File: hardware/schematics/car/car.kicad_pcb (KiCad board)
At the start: 12 copper layers, 17.9 x 30.2 mm, 20 parts, among them M1 Motor_Servo, Q1 PMOS, SW1 SW_SPST, SW2 SW_Push, SW3 SW_Push, U1 VL53L0CXV0DH1, U10 Mini-560, U11 JGA25-37x, U2 VL53L0CXV0DH1, U3 VL53L0CXV0DH1, U4 Pixy2, U6 TB6612FNG, U7 SparkFun OTOS, U9 Mini-360

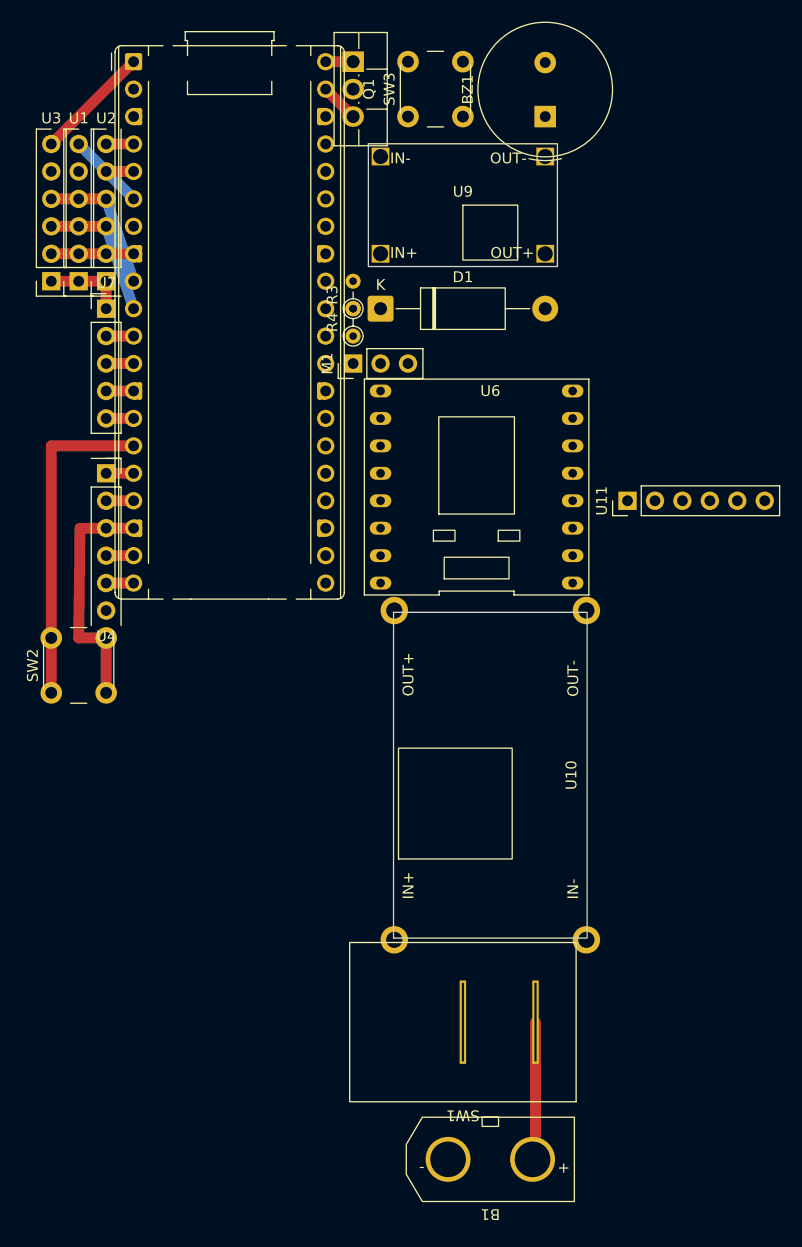
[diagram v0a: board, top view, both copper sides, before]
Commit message: [Schematic] Add ADC cap, place underneath pico it and buzzer.
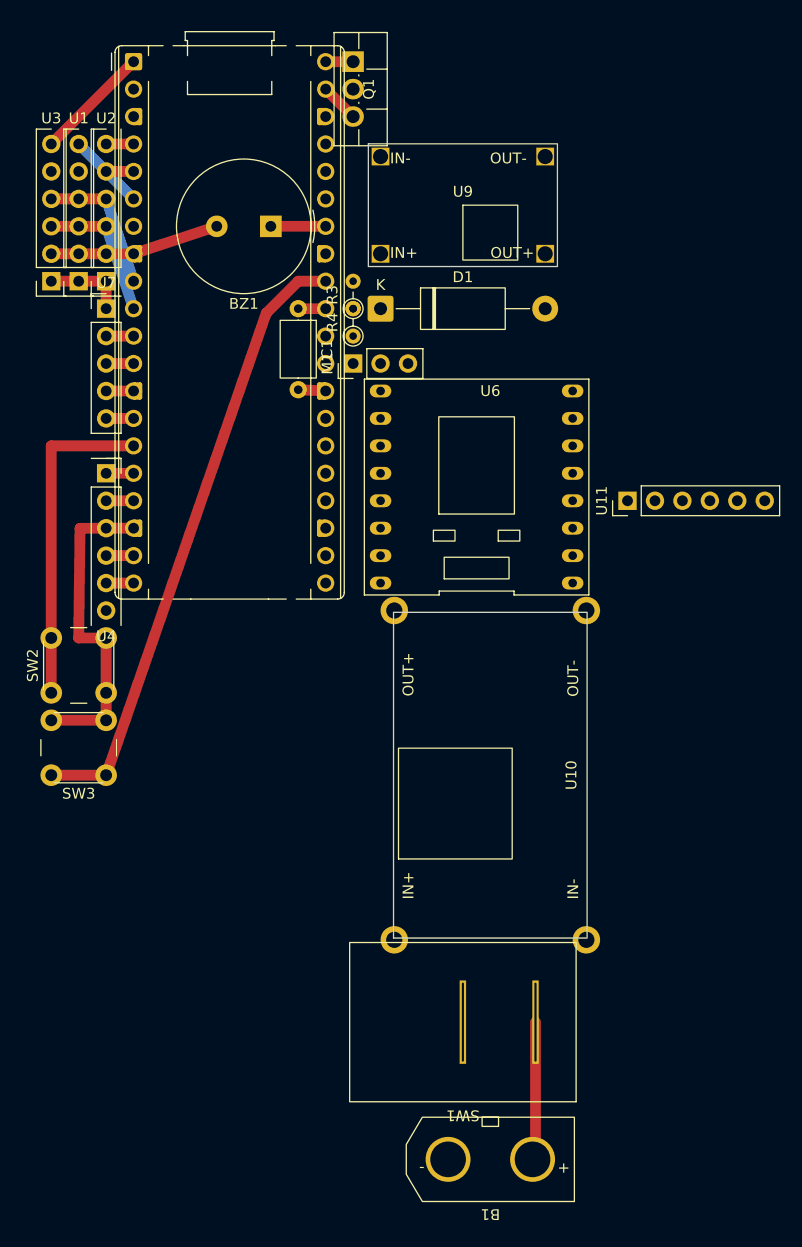
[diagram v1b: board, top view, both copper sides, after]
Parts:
- added C1: 1uF, Capacitor_THT:C_Axial_L5.1mm_D3.1mm_P7.50mm_Horizontal, F.Cu at (142.2, 38.1)
- moved SW3 69.3 mm to (121.9, 78.7), turned to 180 degrees
- moved BZ1 27.4 mm to (139.7, 30.5), turned to 180 degrees
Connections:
- BZ1 pad 1: Net-(A1-GPIO27_ADC1) -> Net-(A1-GPIO28_ADC2)
- SW3 pad 1: Net-(A1-GPIO28_ADC2) -> Net-(A1-GPIO27_ADC1)
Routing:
- net Net-(A1-GPIO27_ADC1): track 0.00 -> 57.1 mm
- net GND: track 152.9 -> 171.2 mm
- net Net-(A1-GPIO28_ADC2): track 0.00 -> 5.08 mm
- net Net-(A1-GPIO26_ADC0): track 0.00 -> 2.54 mm

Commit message: [Schematic] Move a lot, fix mini560 footprint wrong size.
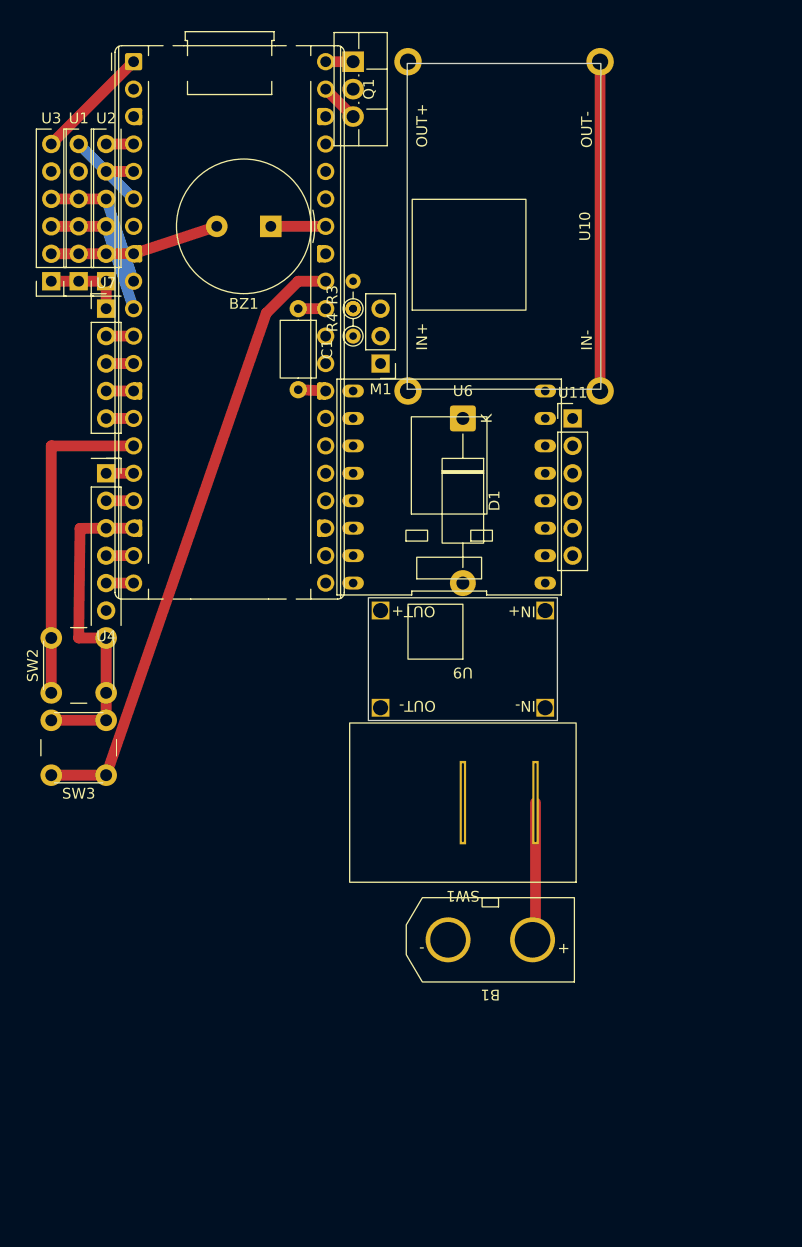
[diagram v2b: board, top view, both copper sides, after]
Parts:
- U11: footprint Connector_PinHeader_2.54mm:PinHeader_1x06_P2.54mm_Vertical -> xlnc-foot:JGA25-37x_PinHeader_1x06_P2.54mm_Vertical
- moved U10 50.8 mm to (161.3, 30.5)
- moved U9 42.0 mm to (157.5, 70.5), turned to 180 degrees
- moved B1 20.3 mm to (160.0, 96.5)
- moved SW1 20.3 mm to (157.5, 83.8)
- moved D1 12.7 mm to (157.5, 48.3), turned to -90 degrees
- moved U11 9.16 mm to (167.6, 48.3), turned to 0 degrees
- moved M1 2.54 mm to (149.9, 43.2), turned to 180 degrees
- moved U6 2.54 mm to (156.2, 54.6)
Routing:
- net GND: track 171.2 -> 241.3 mm
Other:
- board size 17.9 x 30.2 mm -> 17.9 x 30.1 mm

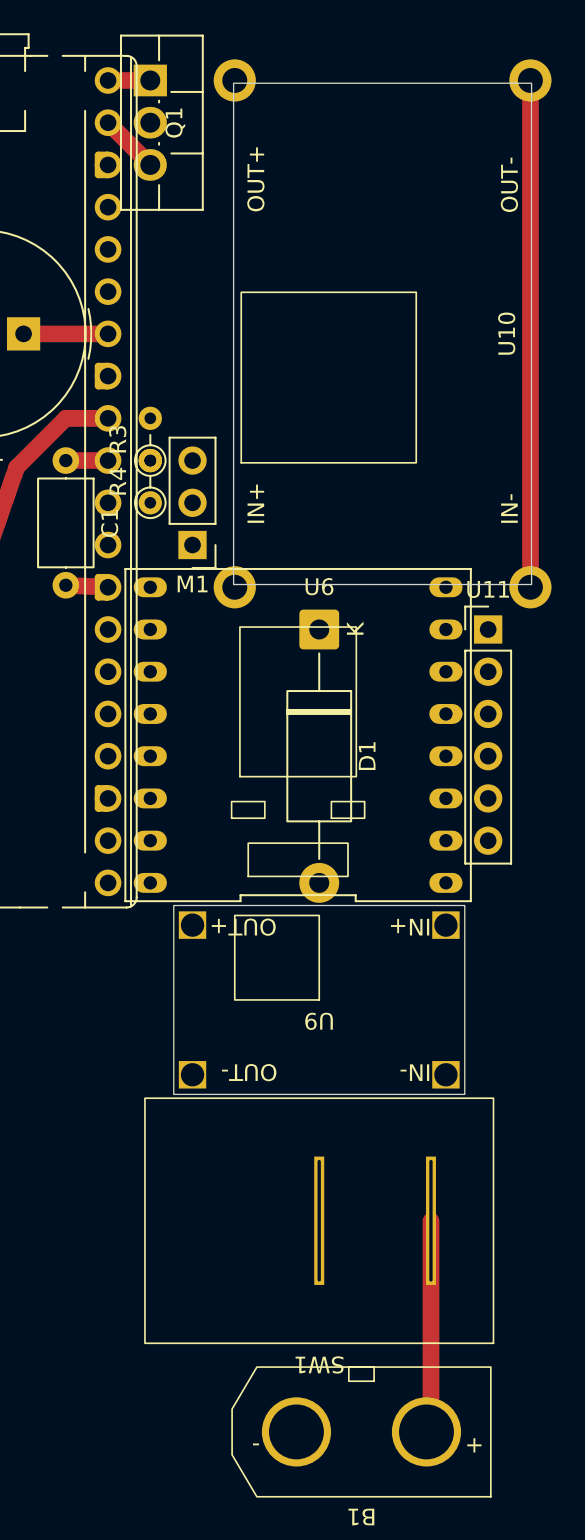
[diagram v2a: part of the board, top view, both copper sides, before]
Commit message: [Schematic] Routed all.
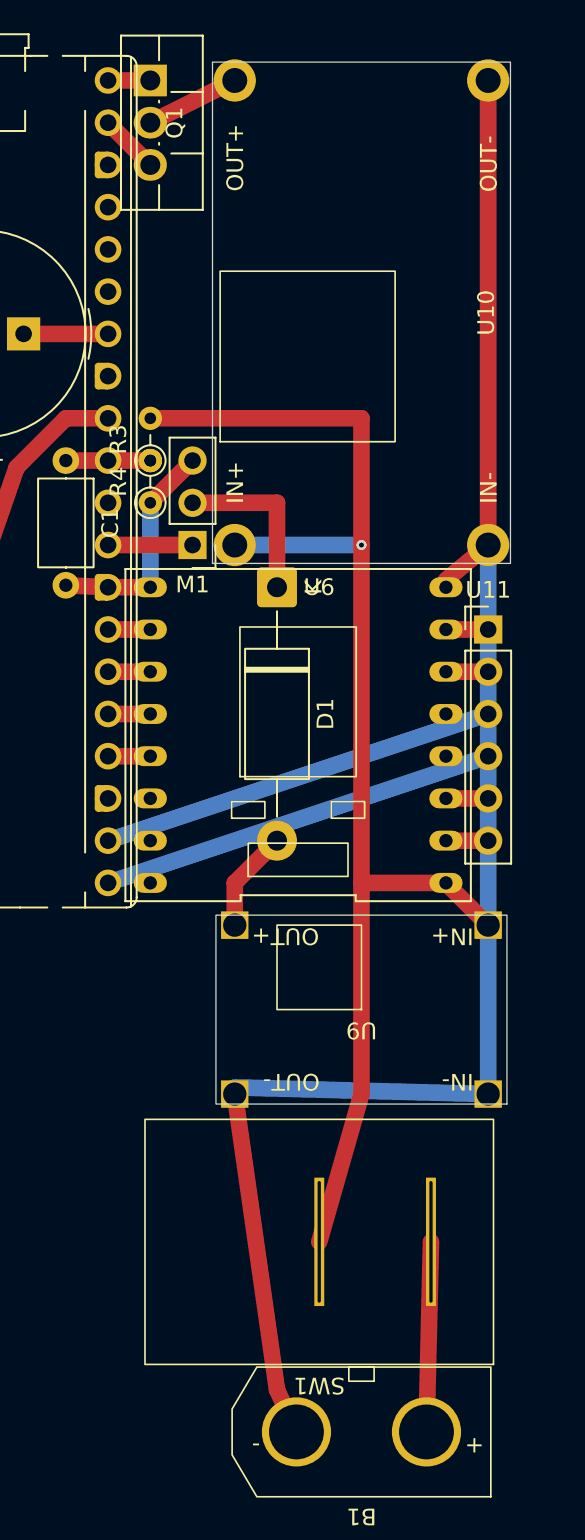
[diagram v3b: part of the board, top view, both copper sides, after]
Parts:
- U9: footprint xlnc-foot:Buck_Mini-360 -> xlnc-foot:Buck_Mini-360_2.54mm
- moved D1 3.59 mm to (154.9, 45.7)
- moved U9 2.61 mm to (160.0, 71.1)
- moved U10 1.80 mm to (160.0, 29.2)
- moved SW1 1.27 mm to (157.5, 85.1)
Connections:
- U11 pad 3: Net-(A1-GPIO20) -> Net-(A1-GPIO16)
- U11 pad 4: Net-(A1-GPIO21) -> Net-(A1-GPIO17)
- U6 pad 1: Net-(U11-M1) -> unconnected-(U6-AO1-Pad1)
- U6 pad 11: unconnected-(U6-BO1-Pad11) -> Net-(U11-M1)
- U6 pad 15: unconnected-(U6-PWMB-Pad15) -> Net-(A1-GPIO21)
- U6 pad 16: unconnected-(U6-BIN2-Pad16) -> Net-(A1-GPIO20)
- U6 pad 17: unconnected-(U6-BIN1-Pad17) -> Net-(A1-GPIO19)
- U6 pad 19: Net-(A1-GPIO16) -> Net-(A1-GPIO18)
- U6 pad 21: Net-(A1-GPIO18) -> unconnected-(U6-AIN1-Pad21)
- U6 pad 22: Net-(A1-GPIO19) -> unconnected-(U6-AIN2-Pad22)
- U6 pad 23: Net-(A1-GPIO17) -> unconnected-(U6-PWMA-Pad23)
- U6 pad 5: Net-(U11-M2) -> unconnected-(U6-AO2-Pad5)
- U6 pad 7: unconnected-(U6-BO2-Pad7) -> Net-(U11-M2)
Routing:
- net VBAT: track 0.00 -> 78.9 mm, vias 0 -> 1
- net GND: track 241.3 -> 318.4 mm
- net +5V: track 0.00 -> 59.1 mm
- net +3.3V: track 30.3 -> 81.2 mm
- net Net-(A1-GPIO17): track 0.00 -> 24.1 mm
- net Net-(A1-GPIO16): track 0.00 -> 24.1 mm
- net Net-(D1-K): track 0.00 -> 9.96 mm
- net +6V: track 0.00 -> 6.13 mm
- net Net-(A1-GPIO22): track 0.00 -> 5.08 mm
- net Net-(U11-M2): track 0.00 -> 2.54 mm
- net Net-(U11-M1): track 0.00 -> 2.54 mm
- net Net-(A1-GPIO26_ADC0): track 2.54 -> 5.08 mm
- net Net-(A1-GPIO21): track 0.00 -> 2.54 mm
- net Net-(A1-GPIO20): track 0.00 -> 2.54 mm
- net Net-(A1-GPIO19): track 0.00 -> 2.54 mm
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
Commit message: [Schematic]  Minor fixes, finishing touches.
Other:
- board size 17.9 x 30.1 mm -> 53.3 x 87.5 mm
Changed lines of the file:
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@@
 		(sheetname "/")
 		(sheetfile "car.kicad_sch")
-		(units
-			(unit
-				(name "A")
-				(pins "1" "2" "3" "4")
-			)
-		)
 		(attr smd)
 		(duplicate_pad_numbers_are_jumpers no)
 		(fp_rect
-			(start -7.755298 -8.5)
-			(end 2.5 2.02431)
+			(start -15.075 -8.96)
+			(end 15.075 8.96)
 			(stroke
-				(width 0.1)
-				(type default)
+				(width 0.05)
+				(type solid)
 			)
 			(fill no)
@@
 		)
 		(fp_rect
-			(start -15.075 -8.96)
-			(end 15.075 8.96)
+			(start -7.755298 -8.5)
+			(end 2.5 2.02431)
 			(stroke
-				(width 0.05)
+				(width 0.1)
 				(type default)
 			)
 			(fill no)
-			(layer "Edge.Cuts")
+			(layer "F.SilkS")
 		)
 		(fp_text user "OUT+"
@@
 			)
 		)
-		(property "Description" "Push button switch, generic, two pins"
+		(property "Description" ""
 			(at 0 0 90)
 			(unlocked yes)
@@
 		(sheetname "/")
 		(sheetfile "car.kicad_sch")
-		(units
-			(unit
-				(name "A")
-				(pins "1" "2")
-			)
-		)
 		(attr through_hole)
 		(duplicate_pad_numbers_are_jumpers no)
@@
 		(model "${KICAD10_3DMODEL_DIR}/Button_Switch_THT.3dshapes/SW_PUSH_6mm.step"
 			(offset
-				(xyz 0 0 0)
+				(xyz -3.14 2.25 0)
 			)
 			(scale
@@
 			)
 			(rotate
-				(xyz 0 0 0)
+				(xyz -0 -0 -0)
 			)
 		)
@@
 		(sheetname "/")
 		(sheetfile "car.kicad_sch")
-		(units
-			(unit
-				(name "A")
-				(pins "1" "2" "3" "4")
-			)
-		)
 		(attr smd)
 		(duplicate_pad_numbers_are_jumpers no)
@@
 			(stroke
 				(width 0.05)
-				(type default)
+				(type solid)
 			)
 			(fill no)
-			(layer "Edge.Cuts")
+			(layer "F.SilkS")
 		)
 		(fp_text user "OUT+"
@@
 		(tags "tact sw push 6mm")
 		(property "Reference" "SW3"
-			(at 0 -4.25 0)
+			(at 0 -4.25 180)
 			(layer "F.SilkS")
 			(effects
@@
 		)
 		(property "Value" "SW_Push"
-			(at 0.5 4.45 0)
+			(at 0.5 4.45 180)
 			(layer "F.Fab")
 			(effects
@@
 			)
 		)
-		(property "Description" "Push button switch, generic, two pins"
+		(property "Description" ""
 			(at 0 0 180)
 			(unlocked yes)
@@
 		(sheetname "/")
 		(sheetfile "car.kicad_sch")
-		(units
-			(unit
-				(name "A")
-				(pins "1" "2")
-			)
-		)
 		(attr through_hole)
 		(duplicate_pad_numbers_are_jumpers no)
@@
 		)
 		(fp_text user "${REFERENCE}"
-			(at 0 0 0)
+			(at 0 0 180)
 			(layer "F.Fab")
 			(effects
@@
 		(model "${KICAD10_3DMODEL_DIR}/Button_Switch_THT.3dshapes/SW_PUSH_6mm.step"
 			(offset
-				(xyz 0 0 0)
+				(xyz -3.14 2.25 0)
 			)
 			(scale
@@
 			)
 			(rotate
-				(xyz 0 0 0)
+				(xyz -0 -0 -0)
 			)
 		)
 	)
+	(gr_rect
+		(start 116.84 14.135)
+		(end 170.18 101.6)
+		(stroke
+			(width 0.05)
+			(type default)
+		)
+		(fill no)
+		(layer "Edge.Cuts")
+	)
 	(segment

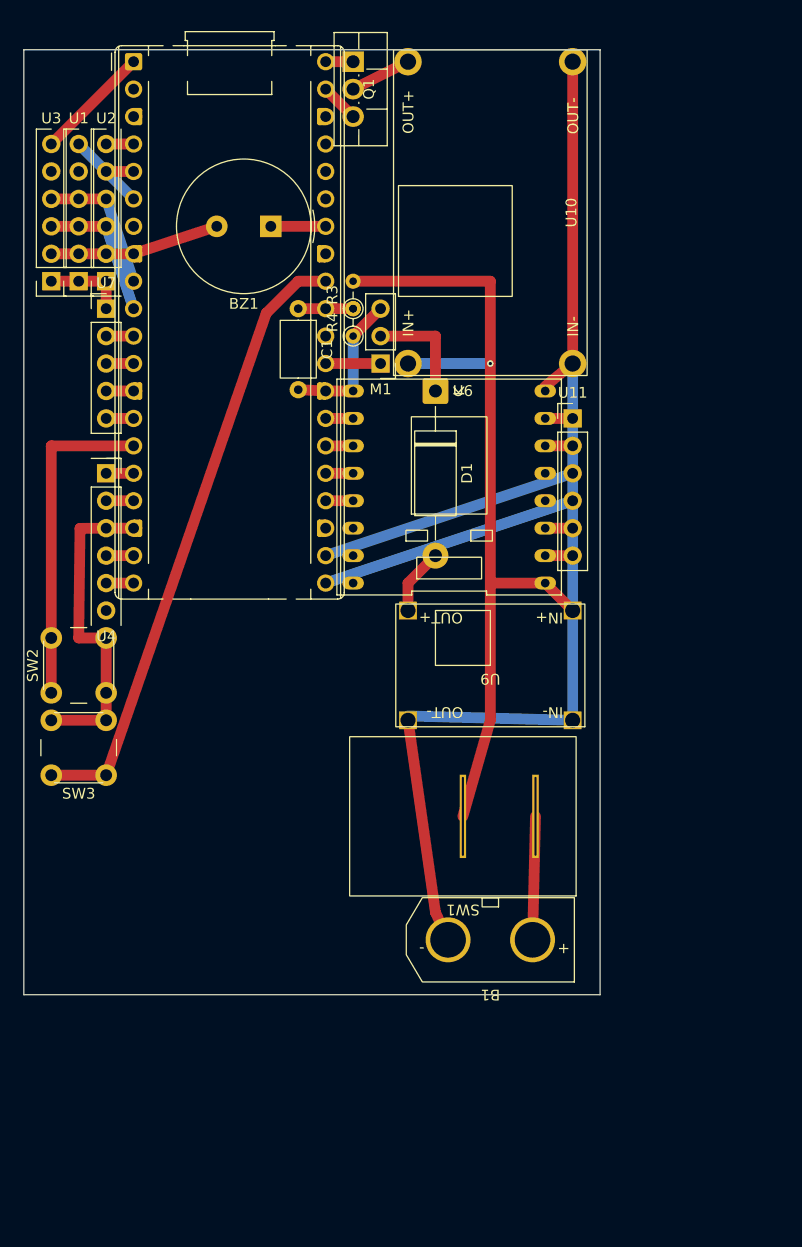
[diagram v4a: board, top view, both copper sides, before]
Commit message: [Schematic] Resize pcb. Ready for review
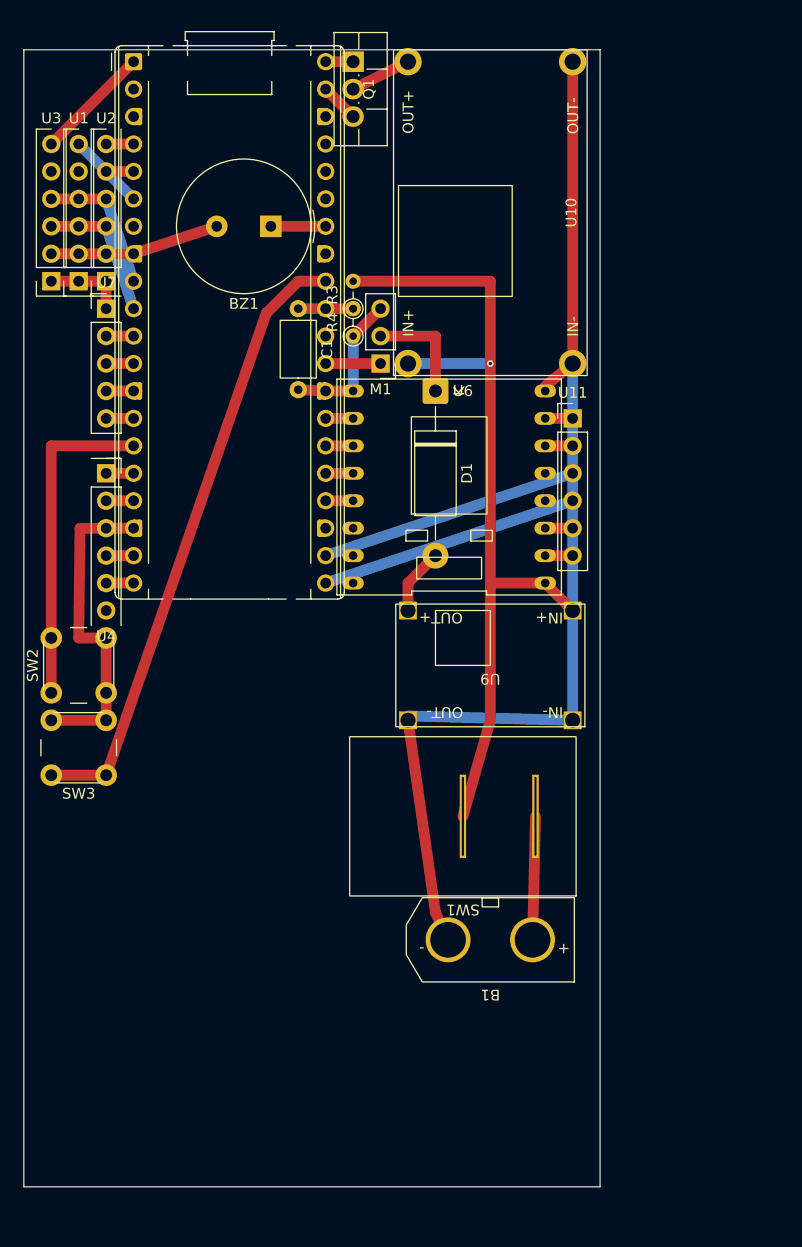
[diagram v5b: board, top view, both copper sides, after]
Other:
- board size 53.3 x 87.5 mm -> 53.3 x 105.2 mm
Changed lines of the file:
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@@
 	(gr_rect
 		(start 116.84 14.135)
-		(end 170.18 101.6)
+		(end 170.18 119.38)
 		(stroke
 			(width 0.05)
